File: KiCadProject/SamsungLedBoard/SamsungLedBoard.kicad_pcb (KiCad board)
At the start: 2 copper layers, 82 x 82 mm, 11 parts, among them J1 XT30

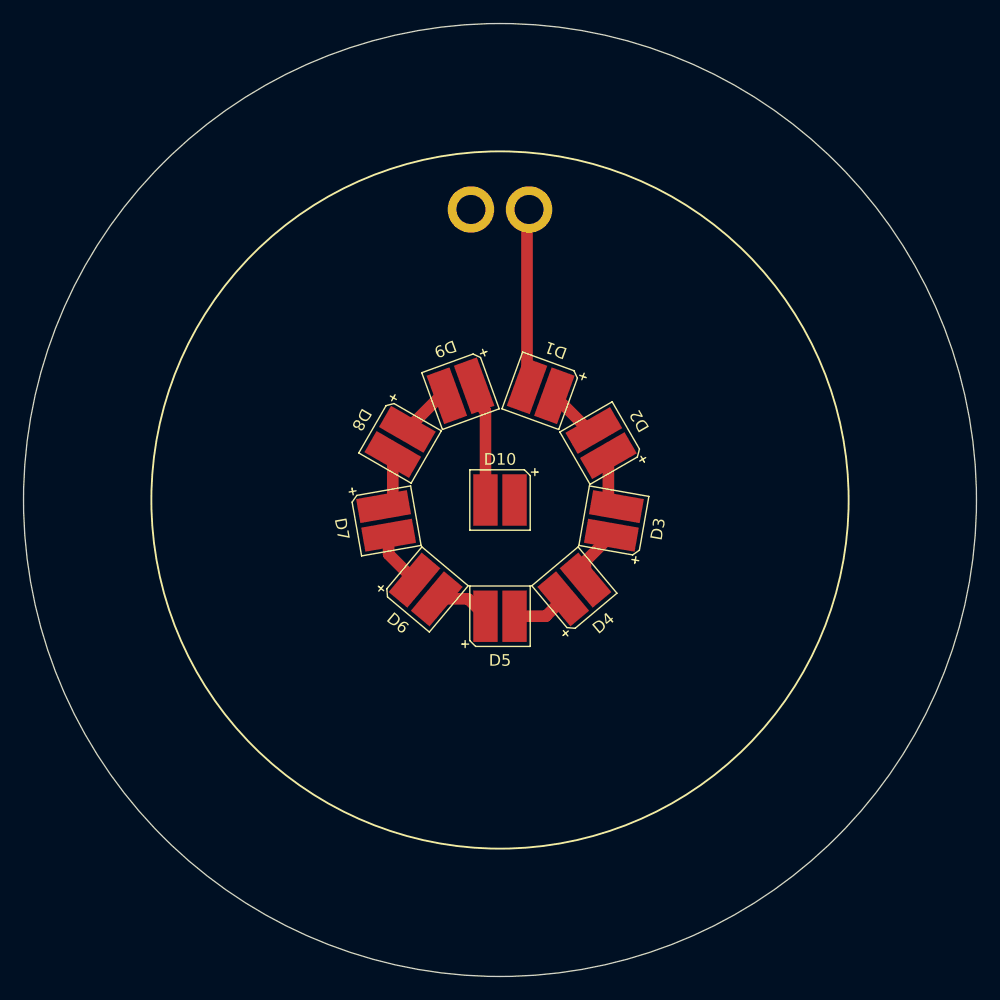
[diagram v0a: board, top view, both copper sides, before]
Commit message: Started on the battery management board
Signed-off-by: Eldalote.Electronics <Eldalote.Electronics@gmail.com>
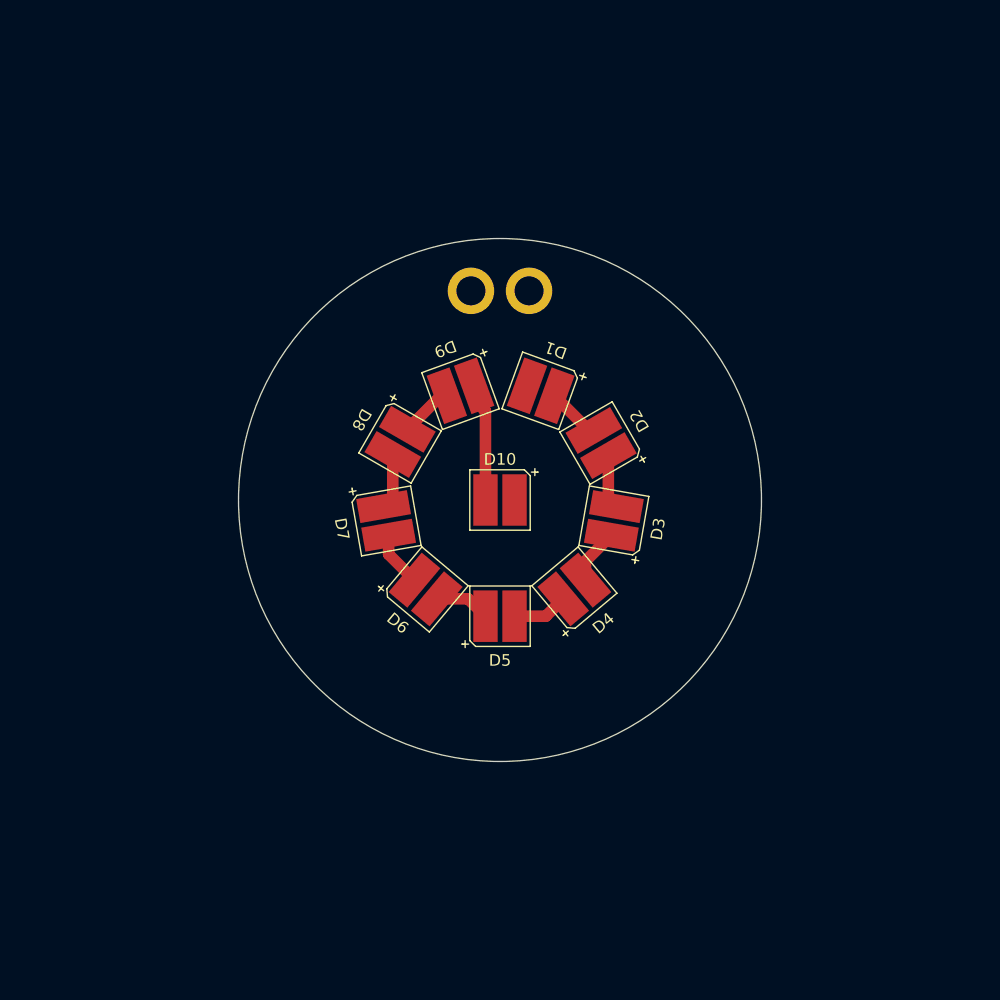
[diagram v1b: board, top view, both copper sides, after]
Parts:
- moved J1 7.00 mm to (150.0, 82.0)
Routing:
- net Net-(D1-Pad1): track 15.7 -> 0.00 mm
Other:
- board size 82 x 82 mm -> 45 x 45 mm
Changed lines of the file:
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@@
   )
   (footprint "Eldalote-footprints:XT30" (layer "B.Cu")
-    (at 150 75 180)
+    (at 150 82 180)
     (property "Sheetfile" "SamsungLedBoard.kicad_sch")
     (property "Sheetname" "")
@@
       (effects (font (size 1 1) (thickness 0.15)) (justify mirror))
     )
-    (fp_line (start -6 0) (end -5 0) (layer "B.SilkS") (width 0.12))
-    (fp_line (start 4.7 0) (end 5.5 0) (layer "B.SilkS") (width 0.12))
-    (fp_line (start -7 1) (end -5 3) (layer "B.SilkS") (width 0.5))
-    (fp_line (start -7 -1) (end -5 -3) (layer "B.SilkS") (width 0.5))
-    (fp_line (start 5.9 3) (end 5.9 -3) (layer "B.SilkS") (width 0.5))
-    (fp_line (start 5.9 -3) (end -5 -3) (layer "B.SilkS") (width 0.5))
-    (fp_line (start 5.1 0.4) (end 5.1 -0.4) (layer "B.SilkS") (width 0.12))
-    (fp_line (start -7 1) (end -7 -1) (layer "B.SilkS") (width 0.5))
-    (fp_line (start 5.9 3) (end -5 3) (layer "B.SilkS") (width 0.5))
+    (fp_line (start 5.85 0.4) (end 5.85 -0.4) (layer "B.SilkS") (width 0.12))
+    (fp_line (start -5.95 -0.85) (end -3.95 -2.85) (layer "B.SilkS") (width 0.2))
+    (fp_line (start 5.45 0) (end 6.25 0) (layer "B.SilkS") (width 0.12))
+    (fp_line (start 5.1 2.85) (end 5.1 -2.85) (layer "B.SilkS") (width 0.2))
+    (fp_line (start -5.4 -0.5) (end -5.4 0.5) (layer "B.SilkS") (width 0.12))
+    (fp_line (start 5.1 2.85) (end -3.95 2.85) (layer "B.SilkS") (width 0.2))
+    (fp_line (start -5.95 0.85) (end -5.95 -0.85) (layer "B.SilkS") (width 0.2))
+    (fp_line (start -5.95 0.85) (end -3.95 2.85) (layer "B.SilkS") (width 0.2))
+    (fp_line (start 5.1 -2.85) (end -3.95 -2.85) (layer "B.SilkS") (width 0.2))
     (pad "1" thru_hole circle (at -2.5 0 180) (size 4 4) (drill 2.5) (layers *.Cu *.Mask)
       (net 1 "Net-(D1-Pad1)") (pinfunction "-") (pintype "passive"))
     (pad "2" thru_hole circle (at 2.5 0 180) (size 4 4) (drill 2.5) (layers *.Cu *.Mask)
       (net 11 "Net-(J1-Pad2)") (pinfunction "+") (pintype "passive"))
+    (model "F:/Engineering/Projects/Divelamp/KiCadProject/3dModels/XT30-male.stp"
+      (offset (xyz 0 0 0))
+      (scale (xyz 1 1 1))
+      (rotate (xyz 0 0 90))
+    )
   )
   (gr_circle (center 150 100) (end 137 100) (layer "B.SilkS") (width 0.16) (fill none))
-  (gr_circle (center 150 100) (end 180 100) (layer "F.SilkS") (width 0.16) (fill none))
-  (gr_circle (center 150 100) (end 191 100) (layer "Edge.Cuts") (width 0.05) (fill none))
-  (segment (start 152.325384 90.172475) (end 152.325384 75.174616) (width 1) (layer "F.Cu") (net 1))
-  (segment (start 152.8 75.3) (end 152.5 75) (width 1) (layer "F.Cu") (net 1))
-  (segment (start 152.325384 75.174616) (end 152.5 75) (width 1) (layer "F.Cu") (net 1))
+  (gr_circle (center 150 100) (end 172.5 100) (layer "Edge.Cuts") (width 0.05) (fill none))
   (segment (start 158.075 94.017468) (end 157.664559 94.017468) (width 1) (layer "F.Cu") (net 2))
   (segment (start 157.664559 94.017468) (end 154.674616 91.027525) (width 1) (layer "F.Cu") (net 2))

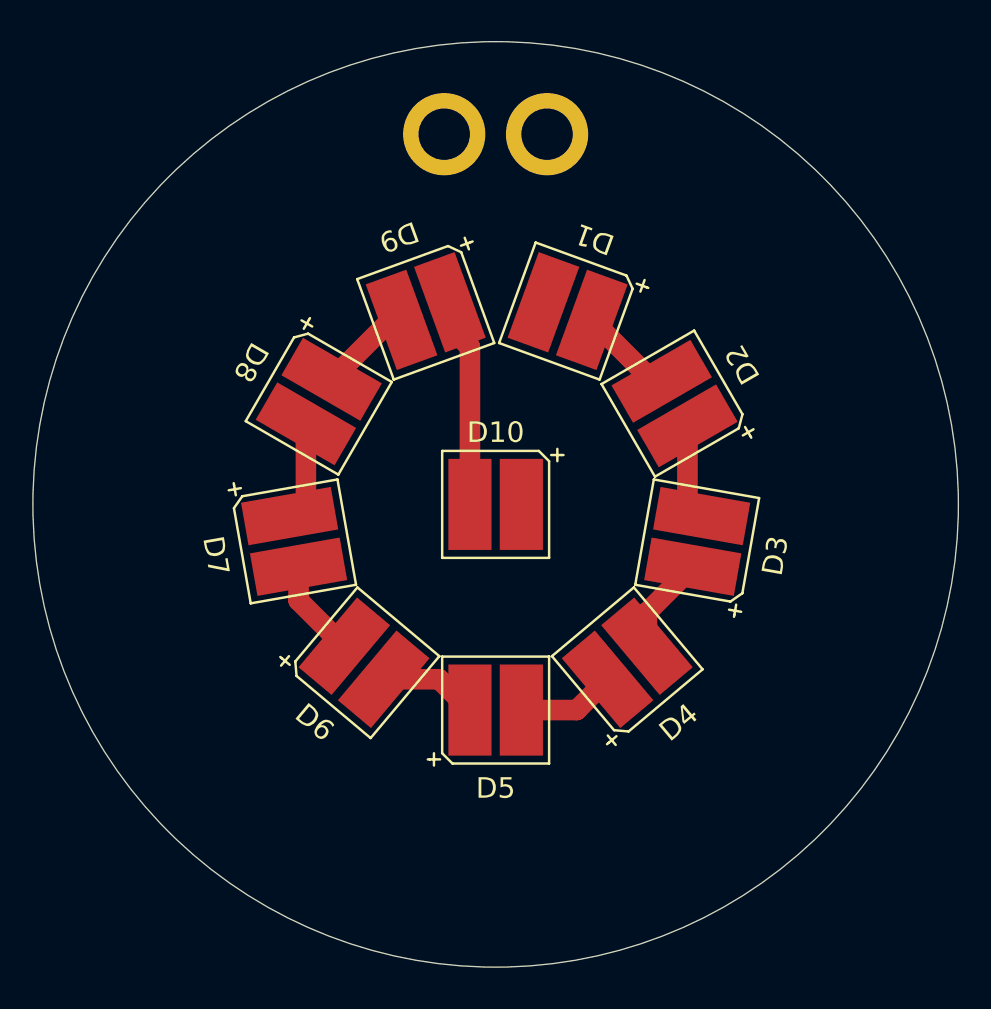
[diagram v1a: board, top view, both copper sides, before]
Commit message: All PCB's should be done. Do a final check before ordering.
Signed-off-by: Eldalote.Electronics <Eldalote.Electronics@gmail.com>
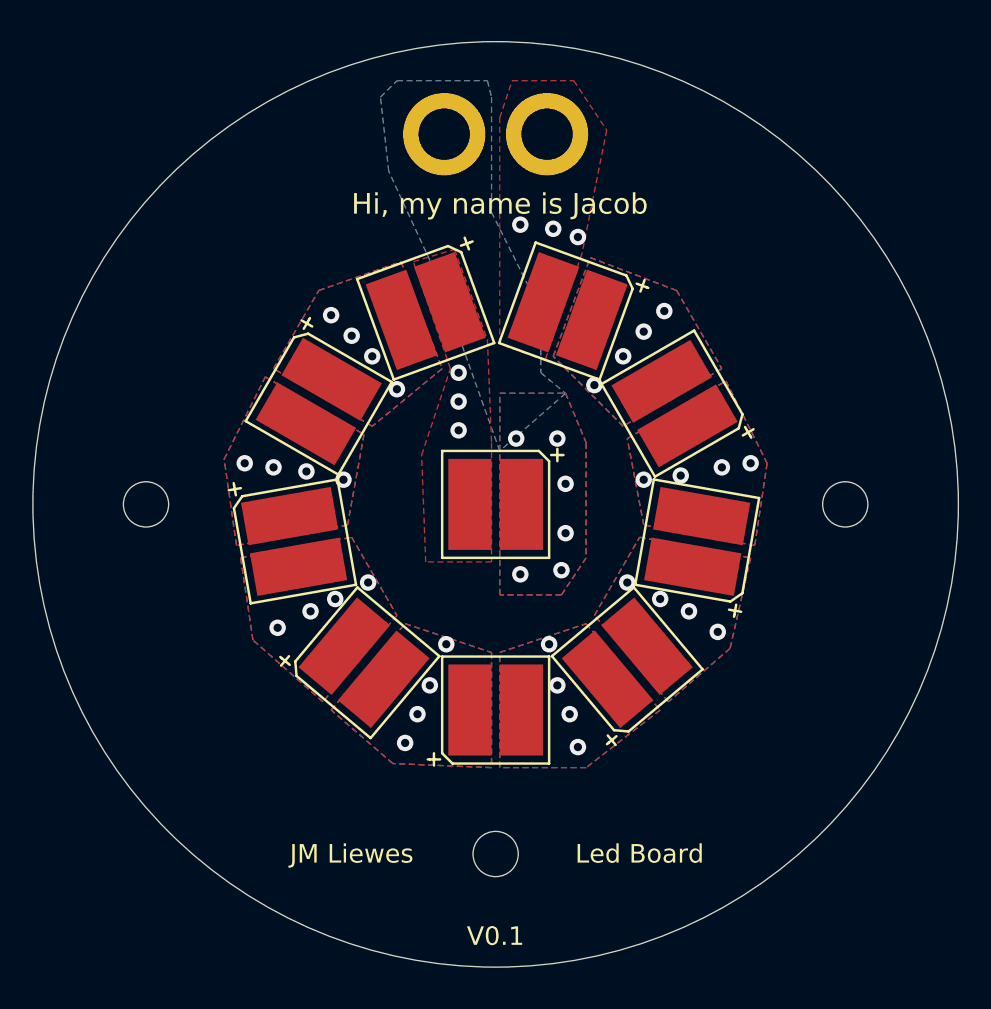
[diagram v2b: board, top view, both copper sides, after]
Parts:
- added REF**: MountingHole_2.2mm_M2, MountingHole:MountingHole_2.2mm_M2, F.Cu at (150.0, 117.0)
- added REF**: MountingHole_2.2mm_M2, MountingHole:MountingHole_2.2mm_M2, F.Cu at (133.0, 100.0)
- added REF**: MountingHole_2.2mm_M2, MountingHole:MountingHole_2.2mm_M2, F.Cu at (167.0, 100.0)
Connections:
- net Net-(D1-Pad1) renamed /L1A
- net Net-(D1-Pad2) renamed /L1-2
- net Net-(D10-Pad1) renamed /L9-10
- net Net-(D2-Pad2) renamed /L2-3
- net Net-(D3-Pad2) renamed /L3-4
- net Net-(D4-Pad2) renamed /L4-5
- net Net-(D5-Pad2) renamed /L5-6
- net Net-(D6-Pad2) renamed /L6-7
- net Net-(D7-Pad2) renamed /L7-8
- net Net-(D8-Pad2) renamed /L8-9
- net Net-(J1-Pad2) renamed /L10C
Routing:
- net /L9-10: track 10.2 -> 0.00 mm, vias 0 -> 3
- net /L7-8: track 4.81 -> 0.00 mm, vias 0 -> 4
- net /L5-6: track 4.81 -> 0.00 mm, vias 0 -> 4
- net /L4-5: track 4.81 -> 0.00 mm, vias 0 -> 4
- net /L6-7: track 4.79 -> 0.00 mm, vias 0 -> 4
- net /L3-4: track 4.79 -> 0.00 mm, vias 0 -> 4
- net /L2-3: track 4.67 -> 0.00 mm, vias 0 -> 4
- net /L1-2: track 4.64 -> 0.00 mm, vias 0 -> 4
- net /L8-9: track 4.60 -> 0.00 mm, vias 0 -> 4
- net /L1A: vias 0 -> 3
- net /L10C: vias 0 -> 6
- added copper zone on B.Cu, net /L1-2
- added copper zone on F.Cu, net /L1-2
- added copper zone on In1.Cu, net /L1-2
- added copper zone on In2.Cu, net /L1-2
- added copper zone on In3.Cu, net /L1-2
- added copper zone on In4.Cu, net /L1-2
- added copper zone on B.Cu, net /L10C
- added copper zone on F.Cu, net /L10C
- added copper zone on In1.Cu, net /L10C
- added copper zone on In2.Cu, net /L10C
- added copper zone on In3.Cu, net /L10C
- added copper zone on In4.Cu, net /L10C
- added copper zone on F.Cu, net /L1A
- added copper zone on In1.Cu, net /L1A
- added copper zone on In2.Cu, net /L1A
- added copper zone on In3.Cu, net /L1A
- added copper zone on In4.Cu, net /L1A
- added copper zone on B.Cu, net /L2-3
- added copper zone on F.Cu, net /L2-3
- added copper zone on In1.Cu, net /L2-3
- added copper zone on In2.Cu, net /L2-3
- added copper zone on In3.Cu, net /L2-3
- added copper zone on In4.Cu, net /L2-3
- added copper zone on B.Cu, net /L3-4
- added copper zone on F.Cu, net /L3-4
- added copper zone on In1.Cu, net /L3-4
- added copper zone on In2.Cu, net /L3-4
- added copper zone on In3.Cu, net /L3-4
- added copper zone on In4.Cu, net /L3-4
- added copper zone on B.Cu, net /L4-5
- added copper zone on F.Cu, net /L4-5
- added copper zone on In1.Cu, net /L4-5
- added copper zone on In2.Cu, net /L4-5
- added copper zone on In3.Cu, net /L4-5
- added copper zone on In4.Cu, net /L4-5
- added copper zone on B.Cu, net /L5-6
- added copper zone on F.Cu, net /L5-6
- added copper zone on In1.Cu, net /L5-6
- added copper zone on In2.Cu, net /L5-6
- added copper zone on In3.Cu, net /L5-6
- added copper zone on In4.Cu, net /L5-6
- added copper zone on B.Cu, net /L6-7
- added copper zone on F.Cu, net /L6-7
- added copper zone on In1.Cu, net /L6-7
- added copper zone on In2.Cu, net /L6-7
- added copper zone on In3.Cu, net /L6-7
- added copper zone on In4.Cu, net /L6-7
- added copper zone on B.Cu, net /L7-8
- added copper zone on F.Cu, net /L7-8
- added copper zone on In1.Cu, net /L7-8
- added copper zone on In2.Cu, net /L7-8
- added copper zone on In3.Cu, net /L7-8
- added copper zone on In4.Cu, net /L7-8
- added copper zone on B.Cu, net /L8-9
- added copper zone on F.Cu, net /L8-9
- added copper zone on In1.Cu, net /L8-9
- added copper zone on In2.Cu, net /L8-9
- added copper zone on In3.Cu, net /L8-9
- added copper zone on In4.Cu, net /L8-9
- added copper zone on F.Cu, net /L9-10
- added copper zone on In1.Cu, net /L9-10
- added copper zone on In2.Cu, net /L9-10
- added copper zone on In3.Cu, net /L9-10
- added copper zone on In4.Cu, net /L9-10
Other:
- copper layers 2 -> 6
- board text added: "Hi, my name is Jacob"
- board text added: "JM Liewes"
- board text added: "Led Board"
- board text added: "V0.1"
- board text added: "jlcjlcjlcjlc"

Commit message: Made ready to order PCBs. Some problems with ordering due to misunderstanding. Thinking about solutions
Signed-off-by: Eldalote.Electronics <Eldalote.Electronics@gmail.com>
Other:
- rule pad_to_mask_clearance: 0.05 -> 0
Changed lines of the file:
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@@
       (dielectric_constraints no)
     )
-    (pad_to_mask_clearance 0.05)
+    (pad_to_mask_clearance 0)
     (pcbplotparams
       (layerselection 0x00010fc_ffffffff)
       (disableapertmacros false)
-      (usegerberextensions false)
+      (usegerberextensions true)
       (usegerberattributes true)
       (usegerberadvancedattributes true)
@@
       (plotinvisibletext false)
       (sketchpadsonfab false)
-      (subtractmaskfromsilk false)
+      (subtractmaskfromsilk true)
       (outputformat 1)
       (mirror false)
-      (drillshape 1)
+      (drillshape 0)
       (scaleselection 1)
-      (outputdirectory "")
+      (outputdirectory "Fab/")
     )
   )
